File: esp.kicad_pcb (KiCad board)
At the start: 2 copper layers, 14 parts, among them U1 ESP32-S2-WROVER, U10 34.81-9024, U11 34.81-8240, U12 34.81-9024, U13 34.81-8240, U14 PCF8574ATS, U2 TCA9548ARGER, U3 TCA9548ARGER, U4 BME280, U5 CCS811, U6 PCF8574ATS, U7 OKI-78SR-12_1.0-W36H-C, U8 OKI-78SR-5_1.5-W36-C, U9 OKI-78SR-3.3_1.5-W36H-C

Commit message: fun
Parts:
- moved U5 145.4 mm to (108.2, 44.4)
- moved U14 144.1 mm to (117.2, 83.8)
- moved U6 143.5 mm to (117.2, 74.0)
- moved U2 61.8 mm to (192.4, 32.3)
- moved U3 60.6 mm to (192.4, 46.5)
- moved U1 60.2 mm to (149.9, 35.6)
- moved U8 25.0 mm to (228.6, 55.9)
- moved U10 7.16 mm to (194.7, 73.7)
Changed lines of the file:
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@@
   (net 149 "unconnected-(U14-P7-Pad20)")
   (footprint "OptoDevice:Finder_34.81" (layer "F.Cu")
-    (at 187.96 76.2)
+    (at 194.65 73.66)
     (descr "Relay SPST, Finder Type 34.81 (opto relays/coupler), vertical/standing form, see https://gfinder.findernet.com/public/attachments/34/EN/S34USAEN.pdf")
     (tags "Relay SPST Finder")
@@
   )
   (footprint "Package_SO:SSOP-20_4.4x6.5mm_P0.65mm" (layer "F.Cu")
-    (at 253.84 30.025)
+    (at 117.2 73.985)
     (descr "SSOP20: plastic shrink small outline package; 20 leads; body width 4.4 mm; (see NXP SSOP-TSSOP-VSO-REFLOW.pdf and sot266-1_po.pdf)")
     (tags "SSOP 0.65")
@@
   )
   (footprint "Converter_DCDC:Converter_DCDC_Murata_OKI-78SR_Vertical" (layer "F.Cu")
-    (at 253.1 60.795)
+    (at 228.6 55.88)
     (descr "https://power.murata.com/data/power/oki-78sr.pdf")
     (tags "78sr3.3 78sr5 78sr9 78sr12 78srXX")
@@
   )
   (footprint "RF_Module:ESP32-S2-WROVER" (layer "F.Cu")
-    (at 209.95 39.325)
+    (at 149.86 35.56)
     (descr "ESP32-S2-WROVER(-I) 2.4 GHz Wi-Fi https://www.espressif.com/sites/default/files/documentation/esp32-s2-wroom_esp32-s2-wroom-i_datasheet_en.pdf")
     (tags "ESP32-S2  ESP32  WIFI")
@@
       (polygon
         (pts
-          (xy 185.95 26.302)
-          (xy 233.95 26.302)
-          (xy 233.95 5.002)
-          (xy 185.95 5.002)
+          (xy 125.86 22.537)
+          (xy 173.86 22.537)
+          (xy 173.86 1.237)
+          (xy 125.86 1.237)
         )
       )
@@
   )
   (footprint "Package_SO:SSOP-20_4.4x6.5mm_P0.65mm" (layer "F.Cu")
-    (at 253.84 38.175)
+    (at 117.2 83.82)
     (descr "SSOP20: plastic shrink small outline package; 20 leads; body width 4.4 mm; (see NXP SSOP-TSSOP-VSO-REFLOW.pdf and sot266-1_po.pdf)")
     (tags "SSOP 0.65")
@@
   )
   (footprint "Package_DFN_QFN:Texas_RGE0024C_EP2.1x2.1mm" (layer "F.Cu")
-    (at 252.81 45.395)
+    (at 192.4375 32.27)
     (descr "Texas  QFN, 24 Pin (http://www.ti.com/lit/ds/symlink/pca9548a.pdf#page=37), generated with kicad-footprint-generator ipc_noLead_generator.py")
     (tags "Texas QFN NoLead")
@@
   )
   (footprint "Package_LGA:AMS_LGA-10-1EP_2.7x4mm_P0.6mm" (layer "F.Cu")
-    (at 251.69 67.405)
+    (at 108.17 44.38)
     (descr "LGA-10, http://ams.com/eng/content/download/951091/2269479/471718")
     (tags "lga land grid array")
@@
   )
   (footprint "Package_DFN_QFN:Texas_RGE0024C_EP2.1x2.1mm" (layer "F.Cu")
-    (at 252.81 51.685)
+    (at 192.4375 46.47)
     (descr "Texas  QFN, 24 Pin (http://www.ti.com/lit/ds/symlink/pca9548a.pdf#page=37), generated with kicad-footprint-generator ipc_noLead_generator.py")
     (tags "Texas QFN NoLead")
@@
     (property "ki_keywords" "Low voltage 8-channel I2C switch with reset")
     (attr smd)
-    (fp_text reference "U3" (at 0 -3.32) (layer "F.SilkS")
-        (effects (font (size 1 1) (thickness 0.15)))
-    )
+    (fp_text reference "U3" (at -60.3725 -16.445) (layer "F.SilkS")
+        (effects (font (size 1 1) (thickness 0.15)))
+    )

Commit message: PCB can be built, naming issues
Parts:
- added D1, D10, D11, D12, D13, D14, D15, D16, D17, D18, D19, D2, D20, D21, D22, D23, D24, D25, D26, D27, D28, D29, D3, D30, D31, D32, D33, D34, D35, D36, D37, D38, D39, D4, D40, D5, D6, D7, D8, D9: 1N4001, Diode_THT:D_DO-41_SOD81_P10.16mm_Horizontal, F.Cu at (256.5, 160.0)
- added J2, J21, J22, J23, J24, J25, J26, J38, J41, J43: 8P8C_Shielded, Connector_RJ:RJ45_HALO_HFJ11-x2450HRL_Horizontal, F.Cu at (82.5, 148.6)
- added J7: Barrel_Jack_MountingPin, Connector_BarrelJack:BarrelJack_SwitchcraftConxall_RAPC10U_Horizontal, F.Cu at (86.4, 39.1)
- added K1: RT314A24, Relay_THT:Relay_1P1T_NO_10x24x18.8mm_Panasonic_ADW11xxxxW_THT, F.Cu at (83.8, 80.6)
- added K10: RT314A24, Relay_THT:Relay_1P1T_NO_10x24x18.8mm_Panasonic_ADW11xxxxW_THT, F.Cu at (114.4, 68.9)
- added K2: RT314A24, Relay_THT:Relay_1P1T_NO_10x24x18.8mm_Panasonic_ADW11xxxxW_THT, F.Cu at (73.7, 75.5)
- added K3: RT314A24, Relay_THT:Relay_1P1T_NO_10x24x18.8mm_Panasonic_ADW11xxxxW_THT, F.Cu at (88.9, 83.1)
- added K4: RT314A24, Relay_THT:Relay_1P1T_NO_10x24x18.8mm_Panasonic_ADW11xxxxW_THT, F.Cu at (86.5, 84.1)
- added K5: RT314A24, Relay_THT:Relay_SPDT_Schrack-RT1-16A-FormC_RM5mm, F.Cu at (175.3, 50.7)
- added K8: RT314A24, Relay_THT:Relay_1P1T_NO_10x24x18.8mm_Panasonic_ADW11xxxxW_THT, F.Cu at (67.5, 83.6)
- added K9: RT314A24, Relay_THT:Relay_1P1T_NO_10x24x18.8mm_Panasonic_ADW11xxxxW_THT, F.Cu at (106.8, 81.6)
- added PS1: RAC20-24SK, Converter_ACDC:Converter_ACDC_Recom_RAC20-xxSK_THT, F.Cu at (20.6, 17.8)
- added Q1: BSS138, Package_TO_SOT_SMD:SOT-23, F.Cu at (162.6, 94.0)
- added U10: PCF8574ATS, Package_SO:SSOP-20_4.4x6.5mm_P0.65mm, F.Cu at (195.9, 99.4)
- added U11: PCA9548ADW, Package_SO:SOIC-24W_7.5x15.4mm_P1.27mm, F.Cu at (124.0, 137.8)
- added U12: PCF8574ATS, Package_SO:SSOP-20_4.4x6.5mm_P0.65mm, F.Cu at (208.3, 101.6)
- added U13: PCF8574ATS, Package_SO:SSOP-20_4.4x6.5mm_P0.65mm, F.Cu at (195.9, 84.1)
- added U14: L298N, Package_TO_SOT_THT:TO-220-15_P2.54x2.54mm_StaggerOdd_Lead4.58mm_Vertical, F.Cu at (242.6, 99.8)
- added U15: PCF8574ATS, Package_SO:SSOP-20_4.4x6.5mm_P0.65mm, F.Cu at (185.4, 116.8)
- added U16: L298N, Package_TO_SOT_THT:TO-220-15_P2.54x2.54mm_StaggerOdd_Lead4.58mm_Vertical, F.Cu at (234.9, 106.7)
- added U17: L298N, Package_TO_SOT_THT:TO-220-15_P2.54x2.54mm_StaggerOdd_Lead4.58mm_Vertical, F.Cu at (247.7, 99.1)
- added U18: NID30S48-24, Converter_DCDC:Converter_DCDC_MeanWell_NID30_THT, F.Cu at (67.2, 52.1)
- added U19: PCA9685PW, Package_SO:TSSOP-28_4.4x9.7mm_P0.65mm, F.Cu at (205.4, 91.7)
- added U20: PCF8574ATS, Package_SO:SSOP-20_4.4x6.5mm_P0.65mm, F.Cu at (201.0, 74.0)
- added U27: L298N, Package_TO_SOT_THT:TO-220-15_P2.54x2.54mm_StaggerOdd_Lead4.58mm_Vertical, F.Cu at (247.7, 86.4)
- added U28: L298N, Package_TO_SOT_THT:TO-220-15_P2.54x2.54mm_StaggerOdd_Lead4.58mm_Vertical, F.Cu at (223.5, 99.1)
- added U29: L298N, Package_TO_SOT_THT:TO-220-15_P2.54x2.54mm_StaggerOdd_Lead4.58mm_Vertical, F.Cu at (240.0, 71.1)
- added U36: PCA9685PW, Package_SO:TSSOP-28_4.4x9.7mm_P0.65mm, F.Cu at (198.1, 111.8)
- added U37: L298N, Package_TO_SOT_THT:TO-220-15_P2.54x2.54mm_StaggerOdd_Lead4.58mm_Vertical, F.Cu at (240.0, 55.9)
- added U38: PCF8574ATS, Package_SO:SSOP-20_4.4x6.5mm_P0.65mm, F.Cu at (208.3, 116.8)
- added U39: PCA9685PW, Package_SO:TSSOP-28_4.4x9.7mm_P0.65mm, F.Cu at (208.3, 63.5)
- added U5: PCF8574ATS, Package_SO:SSOP-20_4.4x6.5mm_P0.65mm, F.Cu at (190.5, 139.7)
- added U6: L298N, Package_TO_SOT_THT:TO-220-15_P2.54x2.54mm_StaggerOdd_Lead4.58mm_Vertical, F.Cu at (252.7, 99.1)
- moved U11 170.1 mm to (39.6, 61.0)
- moved U10 116.3 mm to (128.0, 169.0)
- moved U13 108.8 mm to (128.5, 172.7)
- moved U5 108.2 mm to (205.4, 91.7)
- moved U4 106.1 mm to (200.7, 157.5)
- moved U9 105.2 mm to (147.3, 114.9)
- moved U8 102.1 mm to (238.8, 157.5)
- moved U12 100.9 mm to (133.6, 160.0)
- moved U6 90.0 mm to (205.4, 91.7)
- moved U14 88.6 mm to (205.4, 91.7)
- moved U7 88.5 mm to (165.1, 132.7)
- moved U2 60.8 mm to (205.4, 91.7)
- moved U3 41.1 mm to (164.6, 76.7)
- moved U1 5.98 mm to (150.1, 41.5)
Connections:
- U1 pad 1: GND -> Net-(U1-GND-Pad1)
- U1 pad 13: Net-(U1-IO10) -> unconnected-(U1-IO10-Pad13)
- U1 pad 14: Net-(U1-IO11) -> unconnected-(U1-IO11-Pad14)
- U1 pad 18: Net-(U1-IO15) -> unconnected-(U1-IO15-Pad18)
- U1 pad 21: Net-(U1-IO18) -> unconnected-(U1-IO18-Pad21)
- U1 pad 26: GND -> Net-(U1-GND-Pad1)
- U1 pad 34: unconnected-(U1-IO40-Pad34) -> Net-(U1-IO40)
- U1 pad 35: unconnected-(U1-IO41-Pad35) -> Net-(U1-IO41)
- U1 pad 42: GND -> Net-(U1-GND-Pad1)
- U1 pad 43: GND -> Net-(U1-GND-Pad1)
- U1 pad 5: Net-(U1-IO02) -> unconnected-(U1-IO02-Pad5)
- U1 pad 6: Net-(U1-IO03) -> unconnected-(U1-IO03-Pad6)
- U2 pad 19: Net-(U1-IO03) -> Net-(U1-IO41)
- U2 pad 20: Net-(U1-IO02) -> Net-(U1-IO40)
- U2 pad 9: GND -> unconnected-(U2-GND-Pad9)
- U3 pad 1: unconnected-(U3-SD0-Pad1) -> Net-(U15-SDA)
- U3 pad 16: unconnected-(U3-SD7-Pad16) -> TCA_2_SD7
- U3 pad 17: unconnected-(U3-SC7-Pad17) -> TCA_2_SC7
- U3 pad 19: Net-(U1-IO11) -> Net-(U1-IO17)
- U3 pad 2: unconnected-(U3-SC0-Pad2) -> Net-(U15-SCL)
- U3 pad 20: Net-(U1-IO10) -> Net-(U1-IO16)
- U3 pad 3: unconnected-(U3-SD1-Pad3) -> Net-(U19-SDA)
- U3 pad 4: unconnected-(U3-SC1-Pad4) -> Net-(U19-SCL)
- U3 pad 5: unconnected-(U3-SD2-Pad5) -> Net-(U20-SDA)
- U3 pad 6: unconnected-(U3-SC2-Pad6) -> Net-(U20-SCL)
- U3 pad 9: GND -> unconnected-(U3-GND-Pad9)
- U4 pad 7: GND -> unconnected-(U4-GND-Pad7)
- U7 pad 1: GND -> Net-(BT1-+)
- U7 pad 2: GND -> unconnected-(U7-GND-Pad2)
- U8 pad 1: GND -> Net-(BT1-+)
- U8 pad 2: GND -> unconnected-(U8-GND-Pad2)
- U9 pad 1: GND -> Net-(BT1-+)
- U9 pad 2: GND -> unconnected-(U9-GND-Pad2)

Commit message: slimmed down and spread out pcb
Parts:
- moved U10 110.4 mm to (229.1, 124.7)
- moved U13 110.4 mm to (229.6, 128.4)
- moved U12 110.4 mm to (234.7, 115.7)
- moved U6 90.2 mm to (274.3, 149.9)
- moved U19 66.4 mm to (271.8, 88.9)
- moved J26 65.3 mm to (23.5, 176.4)
- moved J43 62.4 mm to (26.7, 176.4)
- moved J41 59.4 mm to (130.2, 184.0)
- moved J2 58.5 mm to (31.1, 176.4)
- moved J21 58.5 mm to (31.1, 176.4)
- moved J24 55.5 mm to (137.8, 153.6)
- moved J38 54.1 mm to (36.2, 176.4)
- moved J23 47.0 mm to (36.2, 140.9)
- moved U2 46.7 mm to (172.2, 58.9)
- moved J25 45.7 mm to (127.6, 140.9)
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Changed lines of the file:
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@@
   )
   (footprint "OptoDevice:Finder_34.81" placed (layer "F.Cu")
-    (at 128.01 169.0225)
+    (at 229.09 124.685)
     (descr "Relay SPST, Finder Type 34.81 (opto relays/coupler), vertical/standing form, see https://gfinder.findernet.com/public/attachments/34/EN/S34USAEN.pdf")
     (tags "Relay SPST Finder")
@@
   )
   (footprint "OptoDevice:Finder_34.81" placed (layer "F.Cu")
-    (at 128.53 172.72)
+    (at 229.61 128.3825)
     (descr "Relay SPST, Finder Type 34.81 (opto relays/coupler), vertical/standing form, see https://gfinder.findernet.com/public/attachments/34/EN/S34USAEN.pdf")
     (tags "Relay SPST Finder")
@@
   )
   (footprint "Package_SO:SSOP-20_4.4x6.5mm_P0.65mm" placed (layer "F.Cu")
-    (at 205.4175 91.705)
+    (at 274.32 149.86)
     (descr "SSOP20: plastic shrink small outline package; 20 leads; body width 4.4 mm; (see NXP SSOP-TSSOP-VSO-REFLOW.pdf and sot266-1_po.pdf)")
     (tags "SSOP 0.65")
@@
   )
   (footprint "Connector_RJ:RJ45_HALO_HFJ11-x2450HRL_Horizontal" placed (layer "F.Cu")
-    (at 82.55 148.59)
+    (at 137.795 153.565)
     (descr "Halo FastJack, Shielded, https://www.haloelectronics.com/pdf/fastjack-100baset.pdf")
     (tags "10/100 Ethernet RJ45 Tab-Down")
@@
   )
   (footprint "Connector_RJ:RJ45_HALO_HFJ11-x2450HRL_Horizontal" placed (layer "F.Cu")
-    (at 82.55 148.59)
+    (at 59.055 125.625)
     (descr "Halo FastJack, Shielded, https://www.haloelectronics.com/pdf/fastjack-100baset.pdf")
     (tags "10/100 Ethernet RJ45 Tab-Down")
@@
   )
   (footprint "OptoDevice:Finder_34.81" placed (layer "F.Cu")
-    (at 133.61 160.02)
+    (at 234.69 115.6825)
     (descr "Relay SPST, Finder Type 34.81 (opto relays/coupler), vertical/standing form, see https://gfinder.findernet.com/public/attachments/34/EN/S34USAEN.pdf")
     (tags "Relay SPST Finder")
@@
   )
   (footprint "Package_SO:TSSOP-28_4.4x9.7mm_P0.65mm" placed (layer "F.Cu")
-    (at 205.4175 91.705)
+    (at 271.78 88.9)
     (descr "TSSOP, 28 Pin (JEDEC MO-153 Var AE https://www.jedec.org/document_search?search_api_views_fulltext=MO-153), generated with kicad-footprint-generator ipc_gullwing_generator.py")
     (tags "TSSOP SO")
@@
   )
   (footprint "Connector_RJ:RJ45_HALO_HFJ11-x2450HRL_Horizontal" placed (layer "F.Cu")
-    (at 82.55 148.59)
+    (at 36.195 176.425)
     (descr "Halo FastJack, Shielded, https://www.haloelectronics.com/pdf/fastjack-100baset.pdf")
     (tags "10/100 Ethernet RJ45 Tab-Down")
@@
   )
   (footprint "Package_SO:SSOP-20_4.4x6.5mm_P0.65mm" placed (layer "F.Cu")
-    (at 205.4175 91.705)
+    (at 215.9 127)
     (descr "SSOP20: plastic shrink small outline package; 20 leads; body width 4.4 mm; (see NXP SSOP-TSSOP-VSO-REFLOW.pdf and sot266-1_po.pdf)")
     (tags "SSOP 0.65")
@@
   )
   (footprint "Package_DFN_QFN:Texas_RGE0024C_EP2.1x2.1mm" placed (layer "F.Cu")
-    (at 205.4175 91.705)
+    (at 172.195 58.945)
     (descr "Texas  QFN, 24 Pin (http://www.ti.com/lit/ds/symlink/pca9548a.pdf#page=37), generated with kicad-footprint-generator ipc_noLead_generator.py")
     (tags "Texas QFN NoLead")
@@
   )
   (footprint "Connector_RJ:RJ45_HALO_HFJ11-x2450HRL_Horizontal" placed (layer "F.Cu")
-    (at 82.55 148.59)
+    (at 31.115 176.425)
     (descr "Halo FastJack, Shielded, https://www.haloelectronics.com/pdf/fastjack-100baset.pdf")
     (tags "10/100 Ethernet RJ45 Tab-Down")
@@
   )
   (footprint "Connector_RJ:RJ45_HALO_HFJ11-x2450HRL_Horizontal" placed (layer "F.Cu")
-    (at 82.55 148.59)
+    (at 36.195 140.865)
     (descr "Halo FastJack, Shielded, https://www.haloelectronics.com/pdf/fastjack-100baset.pdf")
     (tags "10/100 Ethernet RJ45 Tab-Down")
@@
   )
   (footprint "Package_LGA:AMS_LGA-10-1EP_2.7x4mm_P0.6mm" placed (layer "F.Cu")
-    (at 205.4175 91.705)
+    (at 208.28 91.44)
     (descr "LGA-10, http://ams.com/eng/content/download/951091/2269479/471718")
     (tags "lga land grid array")
@@
   )
   (footprint "Connector_RJ:RJ45_HALO_HFJ11-x2450HRL_Horizontal" placed (layer "F.Cu")
-    (at 82.55 148.59)
+    (at 26.67 176.425)
     (descr "Halo FastJack, Shielded, https://www.haloelectronics.com/pdf/fastjack-100baset.pdf")
     (tags "10/100 Ethernet RJ45 Tab-Down")
@@
   )
   (footprint "Connector_RJ:RJ45_HALO_HFJ11-x2450HRL_Horizontal" placed (layer "F.Cu")
-    (at 82.55 148.59)
+    (at 31.115 176.425)
     (descr "Halo FastJack, Shielded, https://www.haloelectronics.com/pdf/fastjack-100baset.pdf")
     (tags "10/100 Ethernet RJ45 Tab-Down")
@@
   )
   (footprint "Connector_RJ:RJ45_HALO_HFJ11-x2450HRL_Horizontal" placed (layer "F.Cu")
-    (at 82.55 148.59)
+    (at 23.495 176.425)
     (descr "Halo FastJack, Shielded, https://www.haloelectronics.com/pdf/fastjack-100baset.pdf")
     (tags "10/100 Ethernet RJ45 Tab-Down")
@@
   )
   (footprint "Package_SO:SOIC-24W_7.5x15.4mm_P1.27mm" placed (layer "F.Cu")
-    (at 124.03 137.795)
+    (at 103.71 135.255)
     (descr "SOIC, 24 Pin (JEDEC MS-013AD, https://www.analog.com/media/en/package-pcb-resources/package/pkg_pdf/soic_wide-rw/RW_24.pdf), generated with kicad-footprint-generator ipc_gullwing_generator.py")
     (tags "SOIC SO")
@@
   )
   (footprint "Connector_RJ:RJ45_HALO_HFJ11-x2450HRL_Horizontal" placed (layer "F.Cu")
-    (at 82.55 148.59)
+    (at 130.175 184.045)
     (descr "Halo FastJack, Shielded, https://www.haloelectronics.com/pdf/fastjack-100baset.pdf")
     (tags "10/100 Ethernet RJ45 Tab-Down")
@@
   )
   (footprint "Connector_RJ:RJ45_HALO_HFJ11-x2450HRL_Horizontal" placed (layer "F.Cu")
-    (at 82.55 148.59)
+    (at 127.635 140.865)
     (descr "Halo FastJack, Shielded, https://www.haloelectronics.com/pdf/fastjack-100baset.pdf")
     (tags "10/100 Ethernet RJ45 Tab-Down")

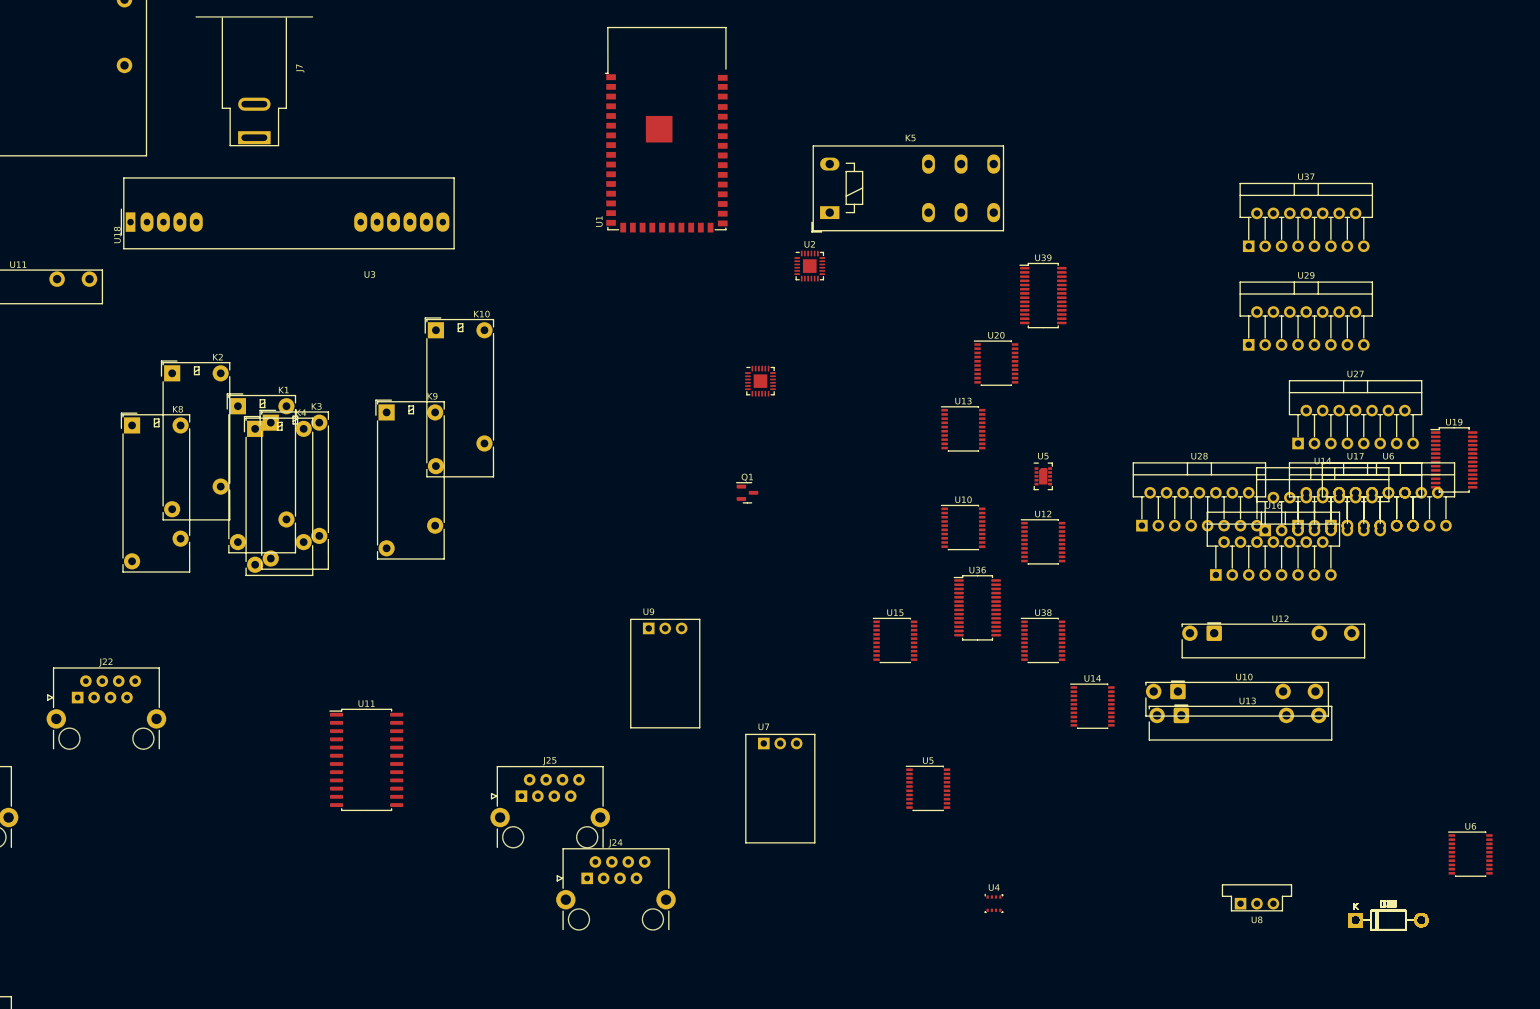
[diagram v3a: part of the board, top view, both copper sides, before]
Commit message: working scematic with seperated layout
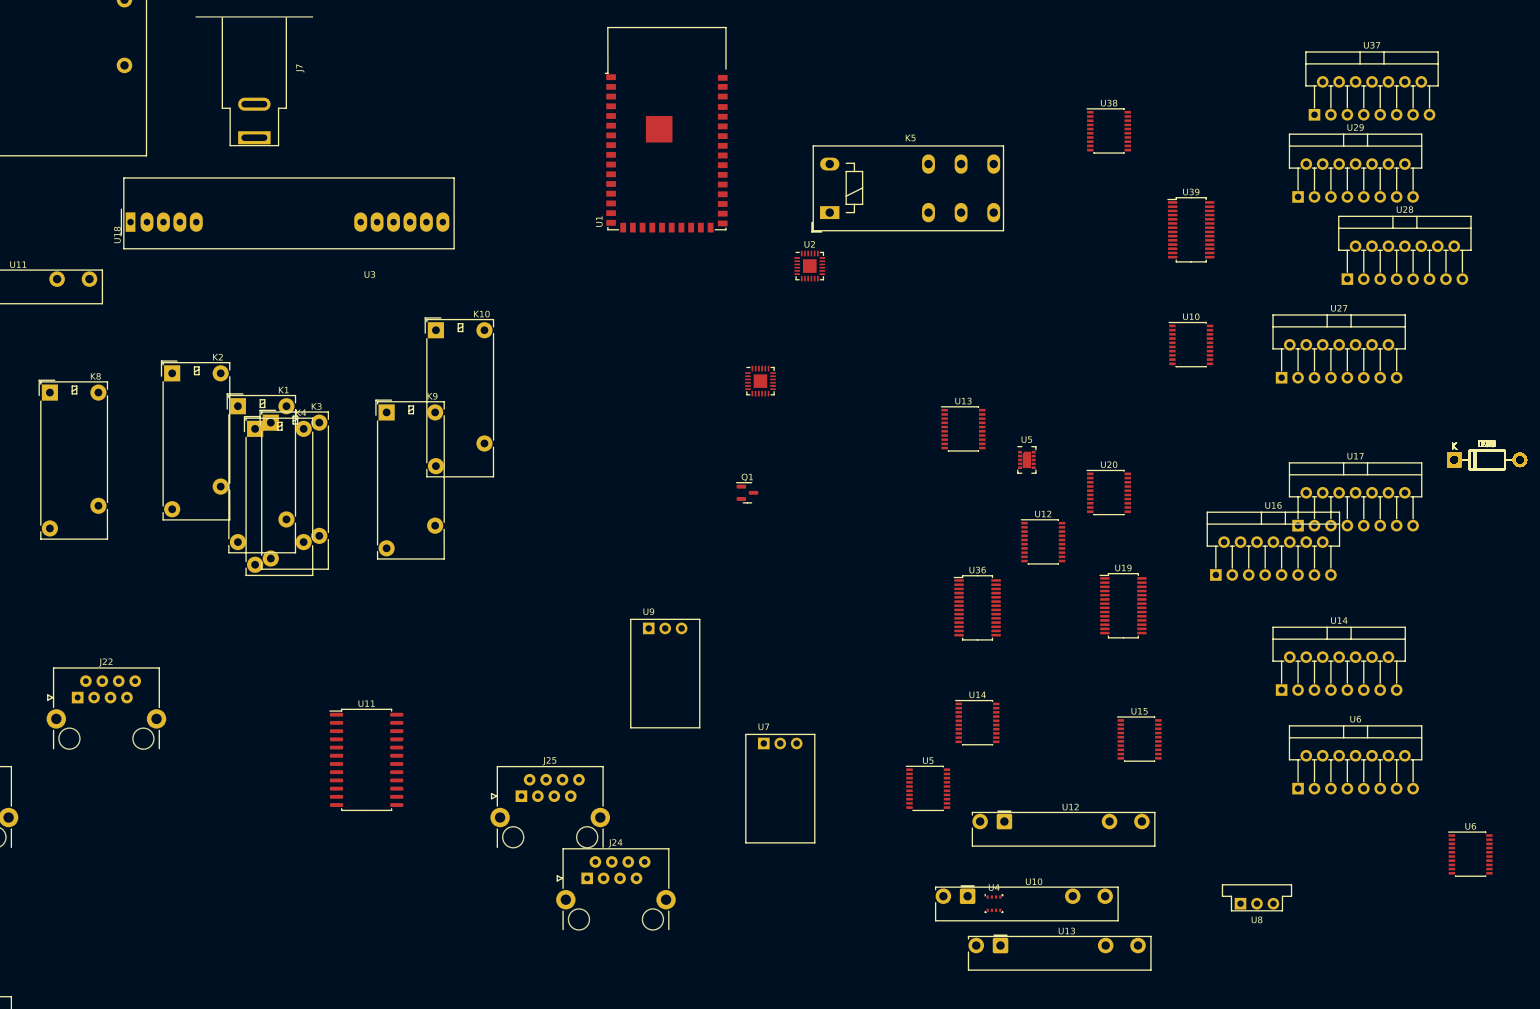
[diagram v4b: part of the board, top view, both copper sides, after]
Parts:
- moved U38 79.4 mm to (218.4, 38.1)
- moved D1 72.7 mm to (271.8, 88.9)
- moved D10 72.7 mm to (271.8, 88.9)
- moved D11 72.7 mm to (271.8, 88.9)
- moved D12 72.7 mm to (271.8, 88.9)
- moved D13 72.7 mm to (271.8, 88.9)
- moved D14 72.7 mm to (271.8, 88.9)
- moved D15 72.7 mm to (271.8, 88.9)
- moved D16 72.7 mm to (271.8, 88.9)
- moved D17 72.7 mm to (271.8, 88.9)
- moved D18 72.7 mm to (271.8, 88.9)
- moved D19 72.7 mm to (271.8, 88.9)
- moved D2 72.7 mm to (271.8, 88.9)
- moved D20 72.7 mm to (271.8, 88.9)
- moved D21 72.7 mm to (271.8, 88.9)
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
